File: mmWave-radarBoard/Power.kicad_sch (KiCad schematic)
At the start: 121 parts, among them J201 Barrel_Jack_Switch, J202 USB_C_Receptacle_USB2.0_16P, Q201 BSS123, U201 TPS628502DRLR, U202 TPD4EUSB30, U203 TPS628502DRLR, U204 TPS2116DRL, U205 TLV75533PDRV, U206 XI6432BRQAAMY

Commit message: Updated schematic
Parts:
- removed NT201, NT202: NetTie_2, symbol Device:NetTie_2
- added FB202, FB204: 30@100MHz 2.2A, symbol Device:FerriteBead
- added FB203: 30@100MHz 4A, symbol Device:FerriteBead
- FB201: value FerriteBead -> 30@100MHz 4A
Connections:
- net FTDI_VBUS: now also FB204.1
- net USB_5V: now also FB202.1
- net at C207.1, C208.1, D203.1 (K)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: now also FB203.1
- net at D202.2 (A), FB201.2: now also FB203.2
- net at D201.2 (A): now also FB202.2
- net at D204.2 (A): now also FB204.2
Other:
- note added: "5V 3A"
- company: Emiel V -> Designer: EV

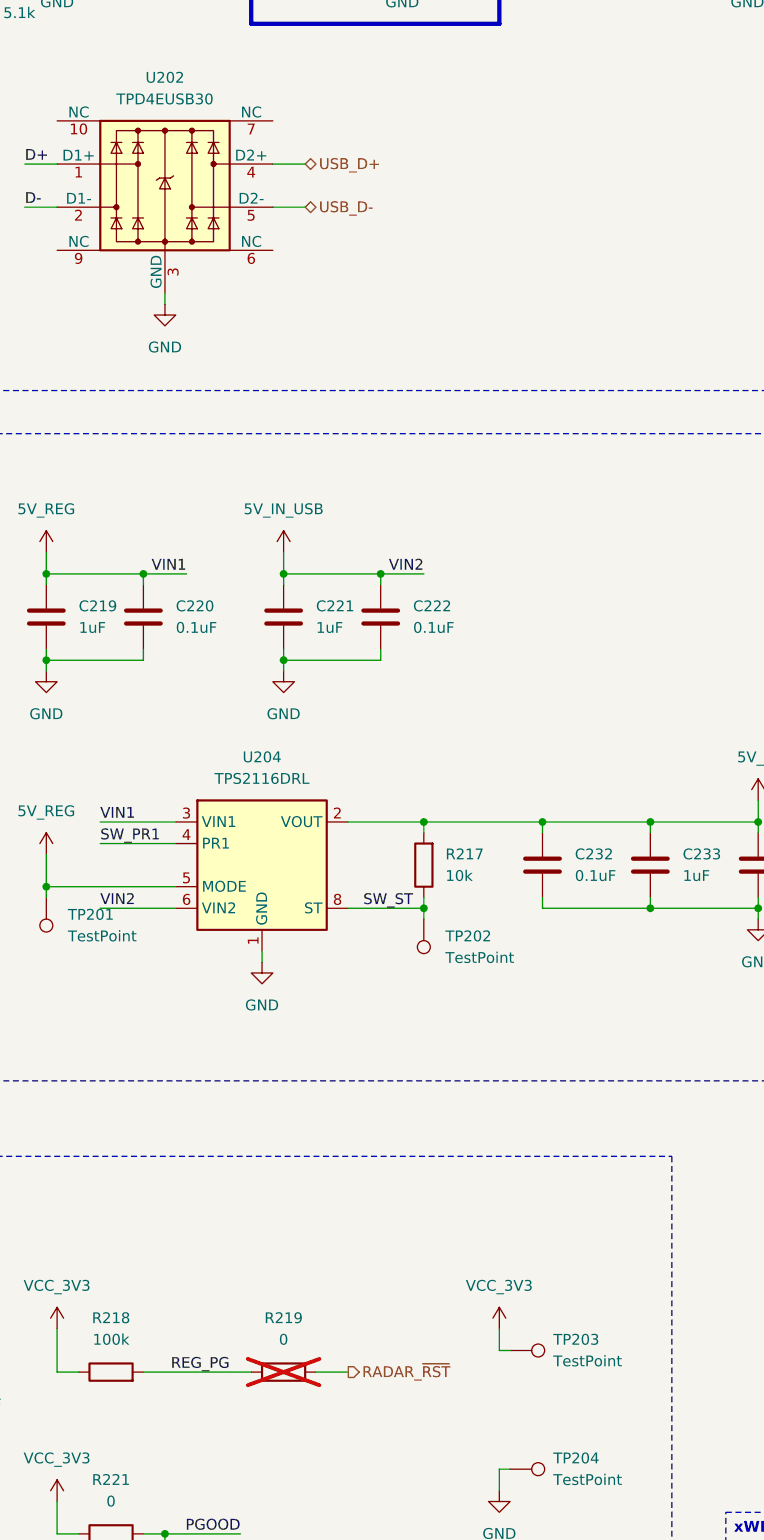
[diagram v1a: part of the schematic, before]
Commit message: Updated schematic of the radar module
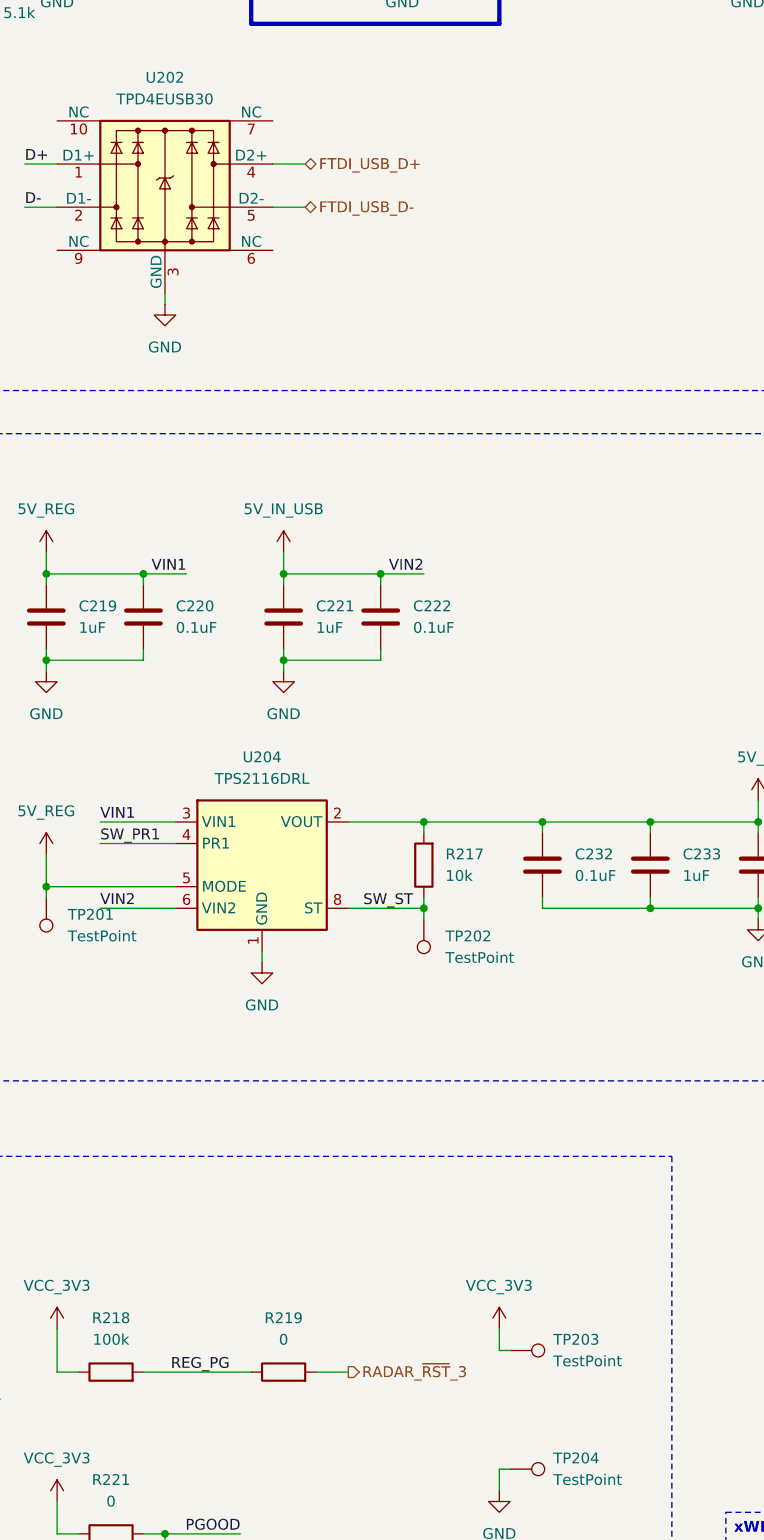
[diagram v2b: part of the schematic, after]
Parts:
- R219: now fitted
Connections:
- net RADAR_~{RST} renamed RADAR_~{RST}_3
- net USB_D+ renamed FTDI_USB_D+
- net USB_D- renamed FTDI_USB_D-
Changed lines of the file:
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@@
 		)
 	)
-	(hierarchical_label "RADAR_~{RST}"
+	(hierarchical_label "RADAR_~{RST}_3"
 		(shape output)
 		(at 134.62 219.71 0)
@@
 		)
 	)
-	(hierarchical_label "USB_D+"
+	(hierarchical_label "FTDI_USB_D+"
 		(shape bidirectional)
 		(at 129.54 77.47 0)
@@
 		)
 	)
-	(hierarchical_label "USB_D-"
+	(hierarchical_label "FTDI_USB_D-"
 		(shape bidirectional)
 		(at 129.54 82.55 0)
@@
 		(in_bom yes)
 		(on_board yes)
-		(dnp yes)
+		(dnp no)
 		(fields_autoplaced yes)
 		(property "Reference" "R219"

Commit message: Removed unnecessary bits
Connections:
- net RADAR_~{RST}_3 renamed RADAR_~{RST}_1
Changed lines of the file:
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@@
 		)
 	)
-	(hierarchical_label "RADAR_~{RST}_3"
+	(hierarchical_label "RADAR_~{RST}_1"
 		(shape output)
 		(at 134.62 219.71 0)

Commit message: Finished schematic
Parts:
- C201, C202, C203, C204, C205, C206: footprint (none) -> Capacitor_SMD:C_0805_2012Metric
- C207, C208: footprint (none) -> Capacitor_SMD:CP_Elec_3x5.3
- C209, C210, C211, C213, C214, C215, C216, C217, C218, C219, C220, C221, C222, C223, C224, C225, C227, C228, C229, C230, C231, C232, C233, C234, C235, C236: footprint (none) -> Capacitor_SMD:C_0603_1608Metric
- C212, C226: footprint (none) -> Capacitor_SMD:C_0402_1005Metric
- C237: renamed from C238; footprint (none) -> Capacitor_SMD:C_0201_0603Metric
- C238: renamed from C239; footprint (none) -> Capacitor_SMD:C_0201_0603Metric
- C239: renamed from C240; footprint (none) -> Capacitor_SMD:C_0402_1005Metric
- C240: renamed from C241; footprint (none) -> Capacitor_SMD:C_0201_0603Metric
- C241: renamed from C242; footprint (none) -> Capacitor_SMD:C_0402_1005Metric
- C242: renamed from C243; footprint (none) -> Capacitor_SMD:C_0201_0603Metric
- C243: renamed from C244; footprint (none) -> Capacitor_SMD:C_0201_0603Metric
- C244: renamed from C245; footprint (none) -> Capacitor_SMD:C_0201_0603Metric
- C245: renamed from C246; footprint (none) -> Capacitor_SMD:C_0201_0603Metric
- C246: renamed from C247; footprint (none) -> Capacitor_SMD:C_0201_0603Metric
- C247: renamed from C248; footprint (none) -> Capacitor_SMD:C_0201_0603Metric
- C248: renamed from C249; footprint (none) -> Capacitor_SMD:C_0201_0603Metric
- C249: renamed from C250; footprint (none) -> Capacitor_SMD:C_0201_0603Metric
- C250: renamed from C251; footprint (none) -> Capacitor_SMD:C_0402_1005Metric
- C251: renamed from C252; footprint (none) -> Capacitor_SMD:C_0201_0603Metric
- C252: renamed from C253; footprint (none) -> Capacitor_SMD:C_0201_0603Metric
- C253: renamed from C254; footprint (none) -> Capacitor_SMD:C_0201_0603Metric
- C254: renamed from C255; footprint (none) -> Capacitor_SMD:C_0201_0603Metric
- C255: renamed from C256; footprint (none) -> Capacitor_SMD:C_0402_1005Metric
- C256: renamed from C257; footprint (none) -> Capacitor_SMD:C_0201_0603Metric
- C257: renamed from C258; footprint (none) -> Capacitor_SMD:C_0402_1005Metric
- C258: renamed from C259; footprint (none) -> Capacitor_SMD:C_0402_1005Metric
- C259: renamed from C260; footprint (none) -> Capacitor_SMD:C_0201_0603Metric
- C260: renamed from C261; footprint (none) -> Capacitor_SMD:C_0201_0603Metric
- C261: renamed from C262; footprint (none) -> Capacitor_SMD:C_0201_0603Metric
- C262: renamed from C263; footprint (none) -> Capacitor_SMD:C_0201_0603Metric
- C263: renamed from C237; footprint (none) -> Capacitor_SMD:C_0402_1005Metric
- D203: footprint (none) -> Diode_SMD:D_SOD-123F
- D204: renamed from D205; footprint (none) -> LED_SMD:LED_0603_1608Metric
- D205: renamed from D206; footprint (none) -> LED_SMD:LED_0603_1608Metric
- F201: footprint (none) -> Fuse:Fuse_1812_4532Metric_Pad1.30x3.40mm_HandSolder
- FB201: renamed from FB203; footprint (none) -> Inductor_SMD:L_0805_2012Metric; now not fitted
- FB202, FB204: footprint (none) -> Inductor_SMD:L_0805_2012Metric
- FB203: renamed from FB201; footprint (none) -> Inductor_SMD:L_0805_2012Metric
- J201: footprint (none) -> Connector_BarrelJack:BarrelJack_GCT_DCJ200-10-A_Horizontal
- J202: footprint Connector_USB:USB_C_Receptacle_GCT_USB4105-xx-A_16P_TopMnt_Horizontal -> Connector_USB:USB_C_Receptacle_G-Switch_GT-USB-7051x
- L201: renamed from L202; footprint (none) -> Inductor_SMD:L_0805_2012Metric
- L202: renamed from L203; footprint (none) -> Inductor_SMD:L_0805_2012Metric
- L203: renamed from L204; footprint (none) -> Inductor_SMD:L_0805_2012Metric
- L204: renamed from L206; footprint (none) -> Inductor_SMD:L_0805_2012Metric
- L205: renamed from L207; footprint (none) -> Inductor_SMD:L_0805_2012Metric
- MOSFET201: footprint (none) -> SSM3K35AMFV:VESM_TOS-L
- R201, R202, R205, R206, R216, R217, R225: footprint (none) -> Resistor_SMD:R_0201_0603Metric
- R203, R204: footprint (none) -> Resistor_SMD:R_0402_1005Metric
- R207: footprint (none) -> Resistor_SMD:R_1206_3216Metric
- R208, R209: footprint (none) -> Resistor_SMD:R_0603_1608Metric
- R210: renamed from R215; footprint (none) -> Resistor_SMD:R_0603_1608Metric
- R211: renamed from R210; footprint (none) -> Resistor_SMD:R_0201_0603Metric
- R212: renamed from R211; footprint (none) -> Resistor_SMD:R_0201_0603Metric
- R213: renamed from R212; footprint (none) -> Resistor_SMD:R_0201_0603Metric
- R214: renamed from R213; footprint (none) -> Resistor_SMD:R_0201_0603Metric
- R215: renamed from R214; footprint (none) -> Resistor_SMD:R_0201_0603Metric
- R218: renamed from R220; footprint (none) -> Resistor_SMD:R_0603_1608Metric
- R219: renamed from R222; footprint (none) -> Resistor_SMD:R_0603_1608Metric
- R220: renamed from R218; footprint (none) -> Resistor_SMD:R_0201_0603Metric
- R221: renamed from R219; footprint (none) -> Resistor_SMD:R_0201_0603Metric
- R222: renamed from R221; footprint (none) -> Resistor_SMD:R_0201_0603Metric
- R223: renamed from R224; footprint (none) -> Resistor_SMD:R_0201_0603Metric
- R224: renamed from R223; footprint (none) -> Resistor_SMD:R_0402_1005Metric
- TP201, TP202, TP203, TP204: footprint (none) -> TestPoint:TestPoint_Pad_D1.0mm
- TP205: renamed from TP209; footprint (none) -> TestPoint:TestPoint_Pad_D1.0mm
- TP206: renamed from TP207; footprint (none) -> TestPoint:TestPoint_Pad_D1.0mm
- TP207: renamed from TP208; footprint (none) -> TestPoint:TestPoint_Pad_D1.0mm
- TP208: renamed from TP205; footprint (none) -> TestPoint:TestPoint_Pad_D1.0mm
- renumbered D204 to D206

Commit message: Updated radar PCB and schematic
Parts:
- removed U202: TPD4EUSB30, Package_SON:USON-10_2.5x1.0mm_P0.5mm, symbol Power_Protection:TPD4EUSB30
- added U207: USBLC6-2P6, Package_TO_SOT_SMD:SOT-666, symbol Power_Protection:USBLC6-2P6
- J202: footprint Connector_USB:USB_C_Receptacle_G-Switch_GT-USB-7051x -> Connector_USB:USB_C_Receptacle_G-Switch_GT-USB-7010ASV
- R218, R219: footprint Resistor_SMD:R_0603_1608Metric -> Resistor_SMD:R_0402_1005Metric
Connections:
- net D+: now also U207.1 (I/O1)
- net D-: now also U207.3 (I/O2)
- net FTDI_USB_D+: now also U207.6 (I/O1)
- net FTDI_USB_D-: now also U207.4 (I/O2)
- net GND: now also U207.2 (GND)
- net USB_5V: now also U207.5 (VBUS)
- net DC_IN: now reaches C207.1, C208.1, D203.1 (K), F201.2, FB201.1, FB203.1
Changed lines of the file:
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@@
 	(wire
 		(pts
+			(xy 240.03 40.64) (xy 240.03 43.18)
+		)
+		(stroke
+			(width 0)
+			(type default)
+		)
+	)
+	(wire
+		(pts
 			(xy 222.25 43.18) (xy 228.6 43.18)
 		)
@@
 	(wire
 		(pts
+			(xy 106.68 71.12) (xy 106.68 72.39)
+		)
+		(stroke
+			(width 0)
+			(type default)
+		)
+	)
+	(wire
+		(pts
 			(xy 257.81 278.13) (xy 257.81 280.67)
 		)
@@
 	(wire
 		(pts
-			(xy 125.73 82.55) (xy 129.54 82.55)
+			(xy 111.76 80.01) (xy 115.57 80.01)
 		)
 		(stroke
@@
 	(wire
 		(pts
-			(xy 125.73 77.47) (xy 129.54 77.47)
+			(xy 111.76 77.47) (xy 115.57 77.47)
 		)
 		(stroke
@@
 	(wire
 		(pts
-			(xy 96.52 82.55) (xy 100.33 82.55)
+			(xy 96.52 80.01) (xy 101.6 80.01)
 		)
 		(stroke
@@
 	(wire
 		(pts
-			(xy 96.52 77.47) (xy 100.33 77.47)
+			(xy 96.52 77.47) (xy 101.6 77.47)
 		)
 		(stroke
@@
 	(wire
 		(pts
-			(xy 113.03 92.71) (xy 113.03 93.98)
+			(xy 106.68 85.09) (xy 106.68 86.36)
 		)
 		(stroke
@@
 	)
 	(label "D-"
-		(at 96.52 82.55 0)
+		(at 96.52 80.01 0)
 		(effects
 			(font
@@
 	(hierarchical_label "FTDI_USB_D+"
 		(shape bidirectional)
-		(at 129.54 77.47 0)
+		(at 115.57 77.47 0)
 		(effects
 			(font
@@
 	(hierarchical_label "FTDI_USB_D-"
 		(shape bidirectional)
-		(at 129.54 82.55 0)
+		(at 115.57 80.01 0)
 		(effects
 			(font
@@
 	)
 	(symbol
+		(lib_id "power:VBUS")
+		(at 106.68 71.12 0)
+		(unit 1)
+		(exclude_from_sim no)
+		(in_bom yes)
+		(on_board yes)
+		(dnp no)
+		(fields_autoplaced yes)
+		(property "Reference" "#PWR0335"
+			(at 106.68 74.93 0)
+			(effects
+				(font
+					(size 1.27 1.27)
+				)
+				(hide yes)
+			)
+		)
+		(property "Value" "USB_5V"
+			(at 106.68 66.04 0)
+			(effects
+				(font
+					(size 1.27 1.27)
+				)
+			)
+		)
+		(property "Footprint" ""
+			(at 106.68 71.12 0)
+			(effects
+				(font
+					(size 1.27 1.27)
+				)
+				(hide yes)
+			)
+		)
+		(property "Datasheet" ""
+			(at 106.68 71.12 0)
+			(effects
+				(font
+					(size 1.27 1.27)
+				)
+				(hide yes)
+			)
+		)
+		(property "Description" "Power symbol creates a global label with name \"VBUS\""
+			(at 106.68 71.12 0)
+			(effects
+				(font
+					(size 1.27 1.27)
+				)
+				(hide yes)
+			)
+		)
+		(pin "1"
+		)
+		(instances
+			(project "mmWave-radarBoard"
+				(path "/65d1bf45-0c7d-403c-8da5-e1777d98e937/63e9aa23-19c0-43a2-8100-8d16d5100cb9"
+					(reference "#PWR0335")
+					(unit 1)
+				)
+			)
+		)
+	)
+	(symbol
 		(lib_id "Device:L")
 		(at 510.54 125.73 90)
@@
 			)
 		)
-		(property "Footprint" "Resistor_SMD:R_0603_1608Metric"
+		(property "Footprint" "Resistor_SMD:R_0402_1005Metric"
 			(at 231.14 164.338 90)
 			(effects
@@
 	)
 	(symbol
+		(lib_id "Power_Protection:USBLC6-2P6")
+		(at 106.68 77.47 0)
+		(unit 1)
+		(exclude_from_sim no)
+		(in_bom yes)
+		(on_board yes)
+		(dnp no)
+		(fields_autoplaced yes)
+		(property "Reference" "U207"
+			(at 108.3311 69.85 0)
+			(effects
+				(font
+					(size 1.27 1.27)
+				)
+				(justify left)
+			)
+		)
+		(property "Value" "USBLC6-2P6"
+			(at 108.3311 72.39 0)
+			(effects
+				(font
+					(size 1.27 1.27)
+				)
+				(justify left)
+			)
+		)
+		(property "Footprint" "Package_TO_SOT_SMD:SOT-666"
+			(at 107.696 84.201 0)
+			(effects
+				(font
+					(size 1.27 1.27)
+					(italic yes)
+				)
+				(justify left)
+				(hide yes)
+			)
+		)
+		(property "Datasheet" "https://www.st.com/resource/en/datasheet/usblc6-2.pdf"
+			(at 107.696 86.106 0)
+			(effects
+				(font
+					(size 1.27 1.27)
+				)
+				(justify left)
+				(hide yes)
+			)
+		)
+		(property "Description" "Very low capacitance ESD protection diode, 2 data-line, SOT-666"
+			(at 106.68 77.47 0)
+			(effects
+				(font
+					(size 1.27 1.27)
+				)
+				(hide yes)
+			)
+		)
+		(pin "1"
+		)
+		(pin "3"
+		)
+		(pin "6"
+		)
+		(pin "4"
+		)
+		(pin "5"
+		)
+		(pin "2"
+		)
+		(instances
+			(project ""
+				(path "/65d1bf45-0c7d-403c-8da5-e1777d98e937/63e9aa23-19c0-43a2-8100-8d16d5100cb9"
+					(reference "U207")
+					(unit 1)
+				)
+			)
+		)
+	)
+	(symbol
 		(lib_id "Device:C")
 		(at 416.56 340.36 0)
@@
 	)
 	(symbol
-		(lib_id "Power_Protection:TPD4EUSB30")
-		(at 113.03 80.01 0)
-		(unit 1)
-		(exclude_from_sim no)
-		(in_bom yes)
-		(on_board yes)
-		(dnp no)
-		(fields_autoplaced yes)
-		(property "Reference" "U202"
-			(at 113.03 67.31 0)
-			(effects
-				(font
-					(size 1.27 1.27)
-				)
-			)
-		)
-		(property "Value" "TPD4EUSB30"
-			(at 113.03 69.85 0)
-			(effects
-				(font
-					(size 1.27 1.27)
-				)
-			)
-		)
-		(property "Footprint" "Package_SON:USON-10_2.5x1.0mm_P0.5mm"
-			(at 88.9 90.17 0)
-			(effects
-				(font
-					(size 1.27 1.27)
-				)
-				(hide yes)
-			)
-		)
-		(property "Datasheet" "http://www.ti.com/lit/ds/symlink/tpd2eusb30a.pdf"
-			(at 113.03 80.01 0)
-			(effects
-				(font
-					(size 1.27 1.27)
-				)
-				(hide yes)
-			)
-		)
-		(property "Description" "4-Channel ESD Protection for Super-Speed USB 3.0 Interface, USON-10"
-			(at 113.03 80.01 0)
-			(effects
-				(font
-					(size 1.27 1.27)
-				)
-				(hide yes)
-			)
-		)
-		(pin "7"
-		)
-		(pin "1"
-		)
-		(pin "9"
-		)
-		(pin "8"
-		)
-		(pin "10"
-		)
-		(pin "6"
-		)
-		(pin "4"
-		)
-		(pin "5"
-		)
-		(pin "3"
-		)
-		(pin "2"
-		)
-		(instances
-			(project ""
-				(path "/65d1bf45-0c7d-403c-8da5-e1777d98e937/63e9aa23-19c0-43a2-8100-8d16d5100cb9"
-					(reference "U202")
-					(unit 1)
-				)
-			)
-		)
-	)
-	(symbol
 		(lib_id "Device:C")
 		(at 486.41 262.89 0)
@@
 	(symbol
 		(lib_id "power:GND")
-		(at 113.03 93.98 0)
+		(at 106.68 86.36 0)
 		(unit 1)
 		(exclude_from_sim no)
@@
 		(fields_autoplaced yes)
 		(property "Reference" "#PWR0224"
-			(at 113.03 100.33 0)
+			(at 106.68 92.71 0)
 			(effects
 				(font
@@
 		)
 		(property "Value" "GND"
-			(at 113.03 99.06 0)
+			(at 106.68 91.44 0)
 			(effects
 				(font
@@
 		)
 		(property "Footprint" ""
-			(at 113.03 93.98 0)
+			(at 106.68 86.36 0)
 			(effects
 				(font
@@
 		)
 		(property "Datasheet" ""
-			(at 113.03 93.98 0)
+			(at 106.68 86.36 0)
 			(effects
 				(font
@@
 		)
 		(property "Description" "Power symbol creates a global label with name \"GND\" , ground"
-			(at 113.03 93.98 0)
+			(at 106.68 86.36 0)
 			(effects
 				(font
@@
 	)
 	(symbol
+		(lib_id "power:VBUS")
+		(at 240.03 40.64 0)
+		(unit 1)
+		(exclude_from_sim no)
+		(in_bom yes)
+		(on_board yes)
+		(dnp no)
+		(fields_autoplaced yes)
+		(property "Reference" "#PWR0334"
+			(at 240.03 44.45 0)
+			(effects
+				(font
+					(size 1.27 1.27)
+				)
+				(hide yes)
+			)
+		)
+		(property "Value" "DC_IN"
+			(at 240.03 35.56 0)
+			(effects
+				(font
+					(size 1.27 1.27)
+				)
+			)
+		)
+		(property "Footprint" ""
+			(at 240.03 40.64 0)
+			(effects
+				(font
+					(size 1.27 1.27)
+				)
+				(hide yes)
+			)
+		)
+		(property "Datasheet" ""
+			(at 240.03 40.64 0)
+			(effects
+				(font
+					(size 1.27 1.27)
+				)
+				(hide yes)
+			)
+		)
+		(property "Description" "Power symbol creates a global label with name \"VBUS\""
+			(at 240.03 40.64 0)
+			(effects
+				(font
+					(size 1.27 1.27)
+				)
+				(hide yes)
+			)
+		)
+		(pin "1"
+		)
+		(instances
+			(project "mmWave-radarBoard"
+				(path "/65d1bf45-0c7d-403c-8da5-e1777d98e937/63e9aa23-19c0-43a2-8100-8d16d5100cb9"
+					(reference "#PWR0334")
+					(unit 1)
+				)
+			)
+		)
+	)
+	(symbol
 		(lib_id "Device:C")
 		(at 351.79 340.36 0)
@@
 			)
 		)
-		(property "Footprint" "Connector_USB:USB_C_Receptacle_G-Switch_GT-USB-7051x"
+		(property "Footprint" "Connector_USB:USB_C_Receptacle_G-Switch_GT-USB-7010ASV"
 			(at 60.96 57.15 0)
 			(effects
@@
 			)
 		)
-		(property "Footprint" "Resistor_SMD:R_0603_1608Metric"
+		(property "Footprint" "Resistor_SMD:R_0402_1005Metric"
 			(at 239.268 171.45 90)
 			(effects

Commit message: Updated schematic and PCB
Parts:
- U201, U203: footprint SOT-5X3-8_DRL_TEX -> TPS62850x:SOT-5X3-8_DRL_TEX
- U205: renamed from U206; footprint FCCSP101_AMY_TEX -> XI6432B:FCCSP101_AMY_TEX
- renumbered C209 to C207, C210 to C208, C211 to C209, C212 to C210, C213 to C211, C214 to C212, C215 to C213, C216 to C214, C217 to C215, C207 to C216, C208 to C217, C223 to C219, C224 to C220, C225 to C221, C226 to C222, C227 to C223, C228 to C224, C229 to C225, C230 to C226, C231 to C227, C219 to C228, C220 to C229, C221 to C230, C222 to C231, C237 to C235, C238 to C236, C239 to C237, C240 to C238, C241 to C239, C242 to C240, C243 to C241, C244 to C242, C245 to C243, C246 to C244, C235 to C245, C236 to C246, R215 to R214, R214 to R215, R224 to R220, R220 to R221, R221 to R222, R222 to R223, R223 to R224, TP205 to TP203, TP206 to TP204, TP203 to TP205, TP204 to TP206, U207 to U202, U205 to U206
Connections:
- net REG_1V2_PG is gone; now on net REG_PG: U201.6 (PG)
- net REG_1V8_PG is gone; now on net REG_PG: U203.6 (PG)
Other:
- moved on the sheet: C201, C202, C203, C204, C205, C206, C207, C208, C209, C210, C211, C212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
